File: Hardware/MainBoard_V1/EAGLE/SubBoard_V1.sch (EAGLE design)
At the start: 17 parts, among them J1 1X2-3.5MM, U1 MAX31855K

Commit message: SubBoard exports
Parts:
- added C2: 10uF, rcl:C-USC0805
- added D1, D2: (no value), adafruit:DIODESOD-523
- added R1, R2: 10k, rcl:R-US_R0402
- C1: value (none) -> 0.01uF
- J5: device SparkFun-Connectors:CONN_02-JST-2-PTH-NO_SILK -> SparkFun-Connectors:CONN_02JST-PTH-2
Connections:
- new net N$4: D1.A, R1.1, U1.SCK
- new net N$6: D2.A, R2.1, U1.!CS
- net 3V3: now also C2.1, R1.2, R2.2, U1.VCC
- net 5V: no longer U1.VCC
- net D5: now also D2.C; no longer U1.!CS
- net D6: now also D1.C; no longer U1.SCK
- net GND: now also C2.2

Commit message: Switch pullups added
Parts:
- added R3, R4: 10K, rcl:R-US_R0402
- C1: LCSC (none) -> C83170
- C2: LCSC (none) -> C89827
- D1, D2: LCSC (none) -> C232841
- FB1, FB2: LCSC (none) -> C883591
- J1: LCSC (none) -> C474892
- J2, J3: LCSC (none) -> C2897378
- J4, J8: LCSC (none) -> C157929
- J5: LCSC (none) -> C173752
- J6: LCSC (none) -> C157923
- J7: LCSC (none) -> C163037
- R1, R2: value 10k -> 10K; LCSC (none) -> C60490
- U1: LCSC (none) -> C52028
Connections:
- net 5V: now also R3.2, R4.2
- net A6: now also R3.1
- net A7: now also R4.1

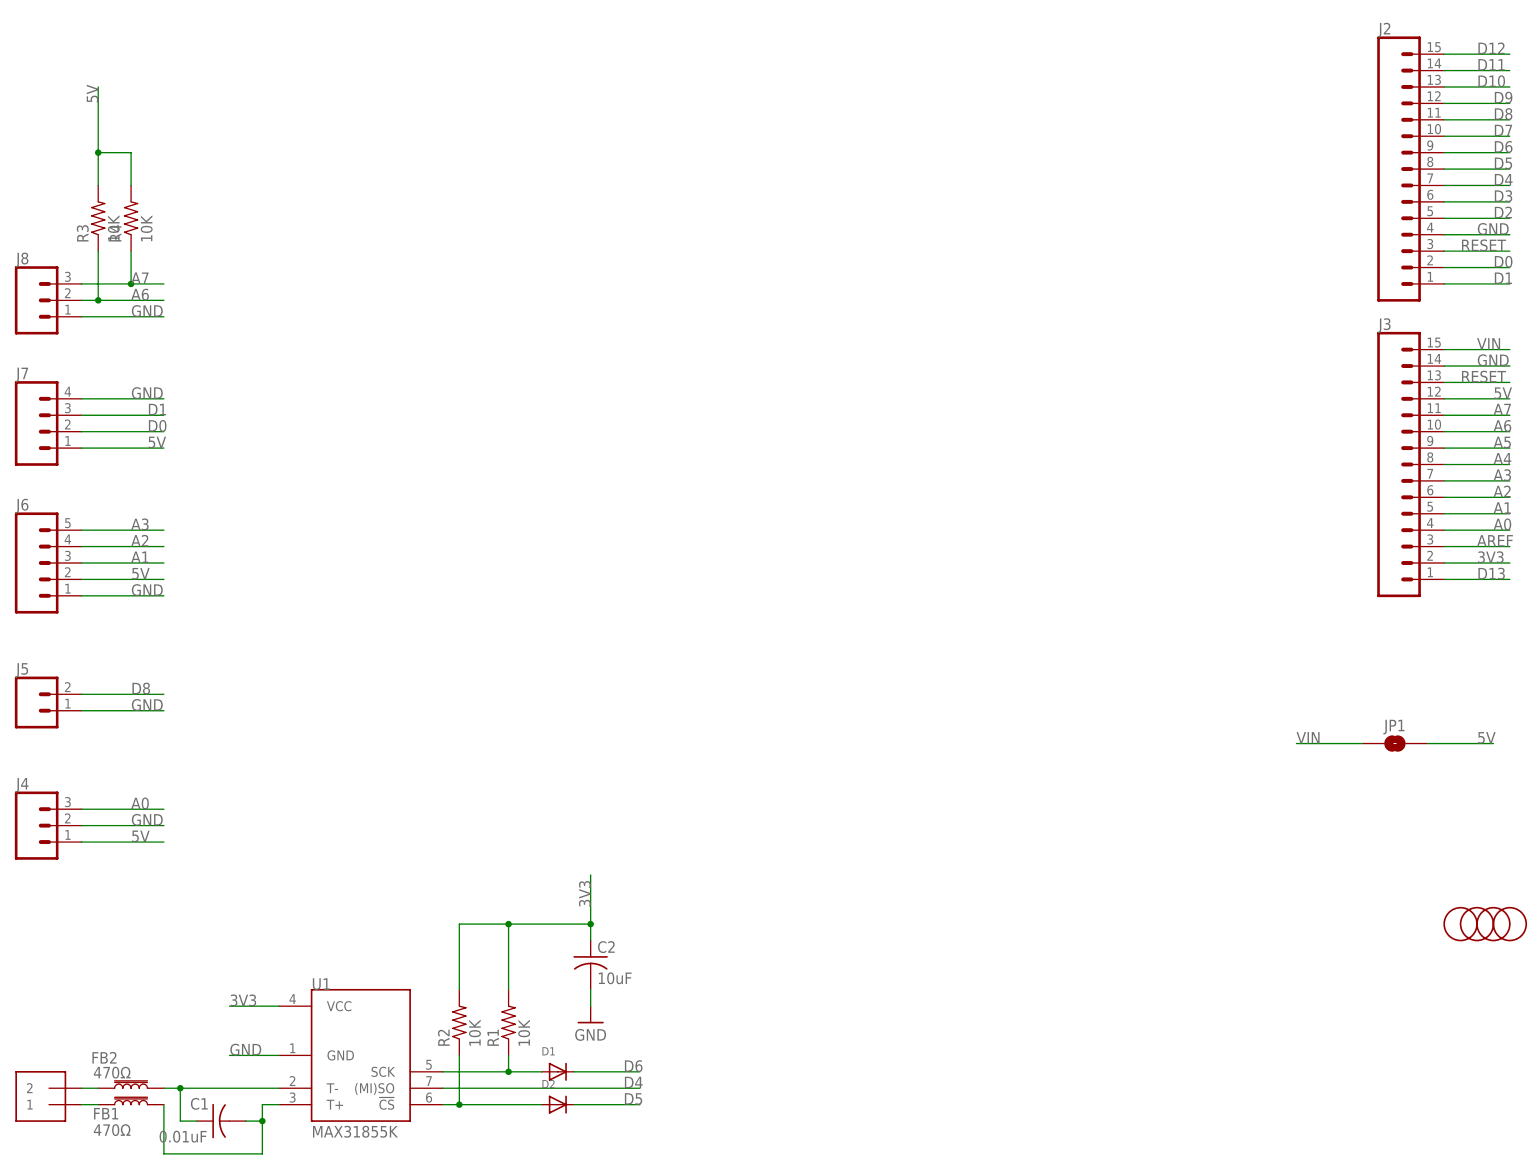
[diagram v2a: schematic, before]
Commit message: Layout change
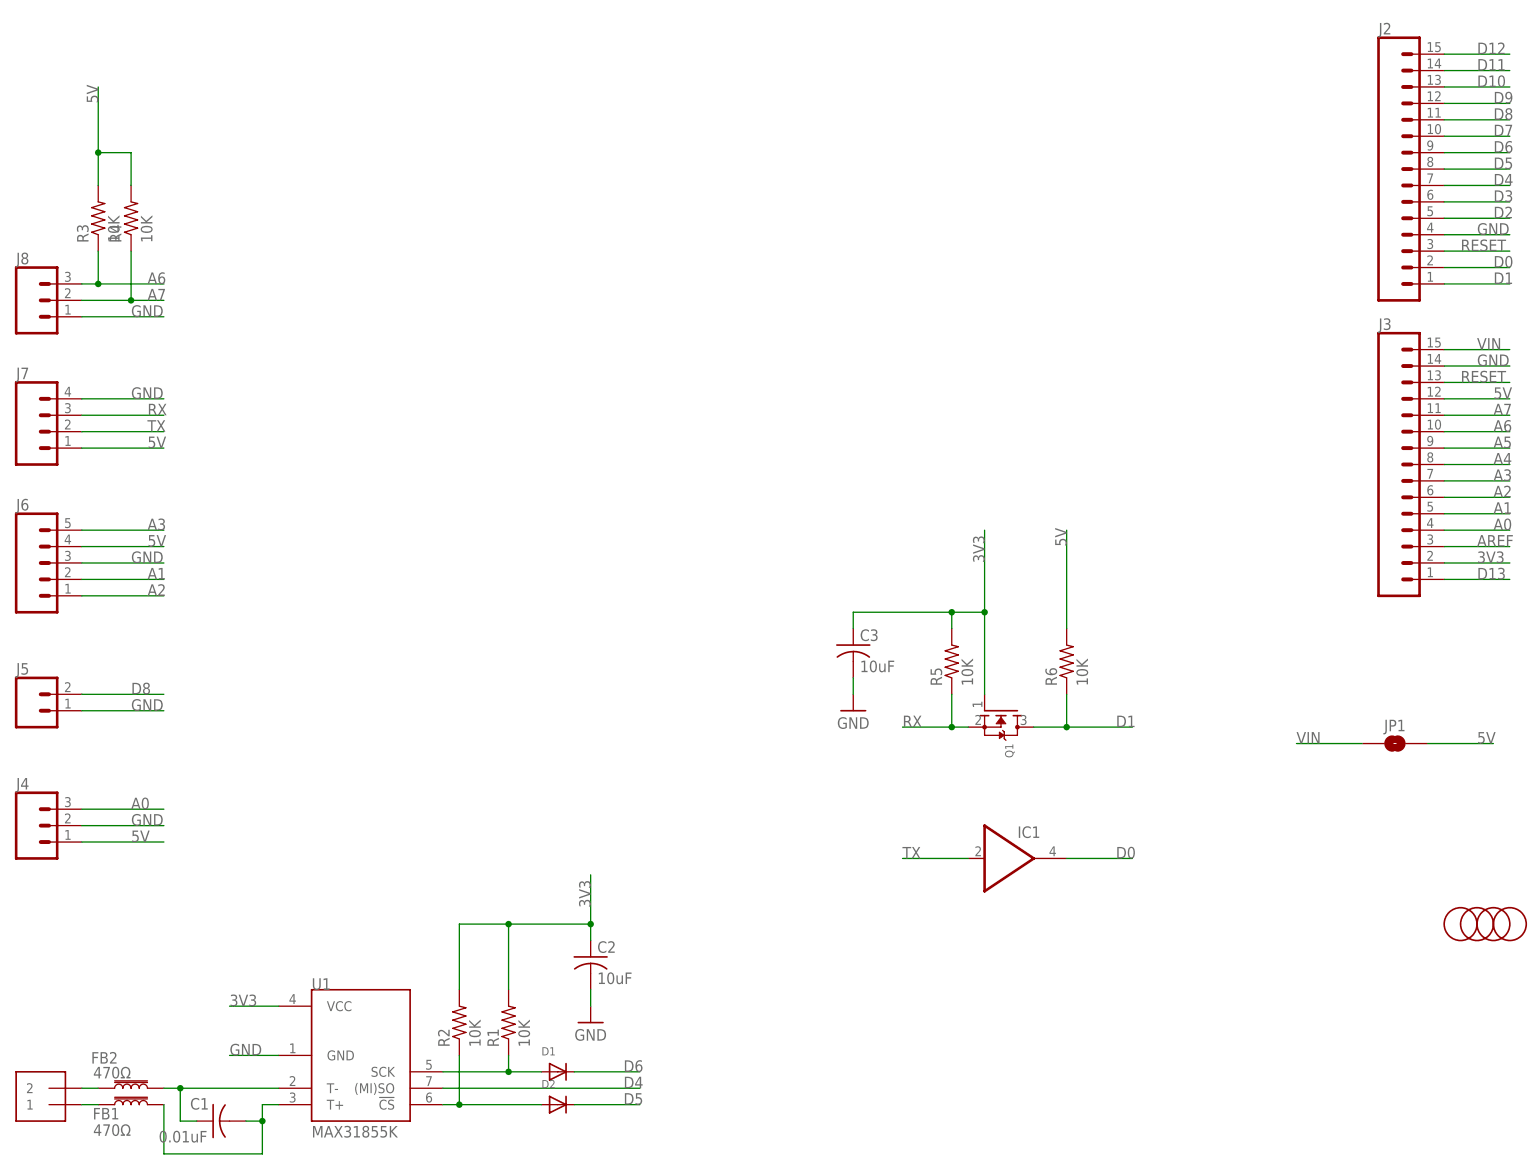
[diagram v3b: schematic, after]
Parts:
- added C3: 10uF, rcl:C-USC0805
- added IC1: 74LVC1G07DBV, 74xx-little-de:74LVC1G07DBV
- added Q1: (no value), adafruit:MOSFET-NREFLOW
- added R5, R6: 10K, rcl:R-US_R0402
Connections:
- new net RX: J7.3, Q1.S, R5.1
- new net TX: IC1A.I, J7.2
- net 3V3: now also C3.1, Q1.G, R5.2
- net 5V: now also J6.4, R6.2; no longer J6.2
- net A1: now also J6.2; no longer J6.3
- net A2: now also J6.1; no longer J6.4
- net A6: now also J8.3; no longer J8.2
- net A7: now also J8.2; no longer J8.3
- net D0: now also IC1A.O; no longer J7.2
- net D1: now also Q1.D, R6.1; no longer J7.3
- net GND: now also C3.2, J6.3; no longer J6.1

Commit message: Boiler SSR pin relocation
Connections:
- net D11: now also J5.2
- net D8: no longer J5.2
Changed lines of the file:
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@@
 <label x="236.22" y="172.72" size="1.778" layer="95"/>
+</segment>
+<segment>
+<pinref part="J5" gate="G$1" pin="2"/>
+<wire x1="20.32" y1="76.2" x2="33.02" y2="76.2" width="0.1524" layer="91"/>
+<label x="27.94" y="76.2" size="1.778" layer="95"/>
 </segment>
 </net>
@@
 <label x="238.76" y="165.1" size="1.778" layer="95"/>
 </segment>
-<segment>
-<pinref part="J5" gate="G$1" pin="2"/>
-<wire x1="20.32" y1="76.2" x2="33.02" y2="76.2" width="0.1524" layer="91"/>
-<label x="27.94" y="76.2" size="1.778" layer="95"/>
-</segment>
 </net>

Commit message: Nextion full buffer IO
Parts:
- removed Q1: (no value), adafruit:MOSFET-NREFLOW
- removed R5, R6: 10K, rcl:R-US_R0402
- added C4: 10uF, rcl:C-USC0603
- added IC2: 74LVC1G07DBV, 74xx-little-de:74LVC1G07DBV
- C1: device rcl:C-USC0805 -> rcl:C-USC0603; LCSC C83170 -> C1589
- C2, C3: device rcl:C-USC0805 -> rcl:C-USC0603; LCSC C89827 -> C19702
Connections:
- net 3V3: no longer Q1.G, R5.2
- net 5V: now also C4.1; no longer R6.2
- net D1: now also IC2A.I; no longer Q1.D, R6.1
- net GND: now also C4.2
- net RX: now also IC2A.O; no longer Q1.S, R5.1
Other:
- moved on the sheet: C3

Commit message: Switch reassignment
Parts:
- removed R4: 10K, rcl:R-US_R0402
- added C5: 0.1uF, rcl:C-USC0603
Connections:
- net 3V3: now also C5.1, R3.1
- net 5V: no longer R3.2, R4.2
- net A6: no longer J8.3, R3.1
- net A7: no longer J8.2, R4.1
- net D7: now also J8.2
- net D8: now also J8.3
- net GND: now also C5.2
- net TX: now also R3.2
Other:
- moved on the sheet: C4, IC1, IC2, R3
